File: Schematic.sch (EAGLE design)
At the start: 63 parts, among them IC1 7812, IC2 LM358N, Q1 IRF3205, Q2 IRF3205, Q3 IRF3205, Q4 IRF3205, Q5 IRF3205, Q6 IRF3205, Q7 IRF3205, Q8 IRF3205, X1 12Vcc IN, X2 MOTOR DC, X3 Resistencia Shunt

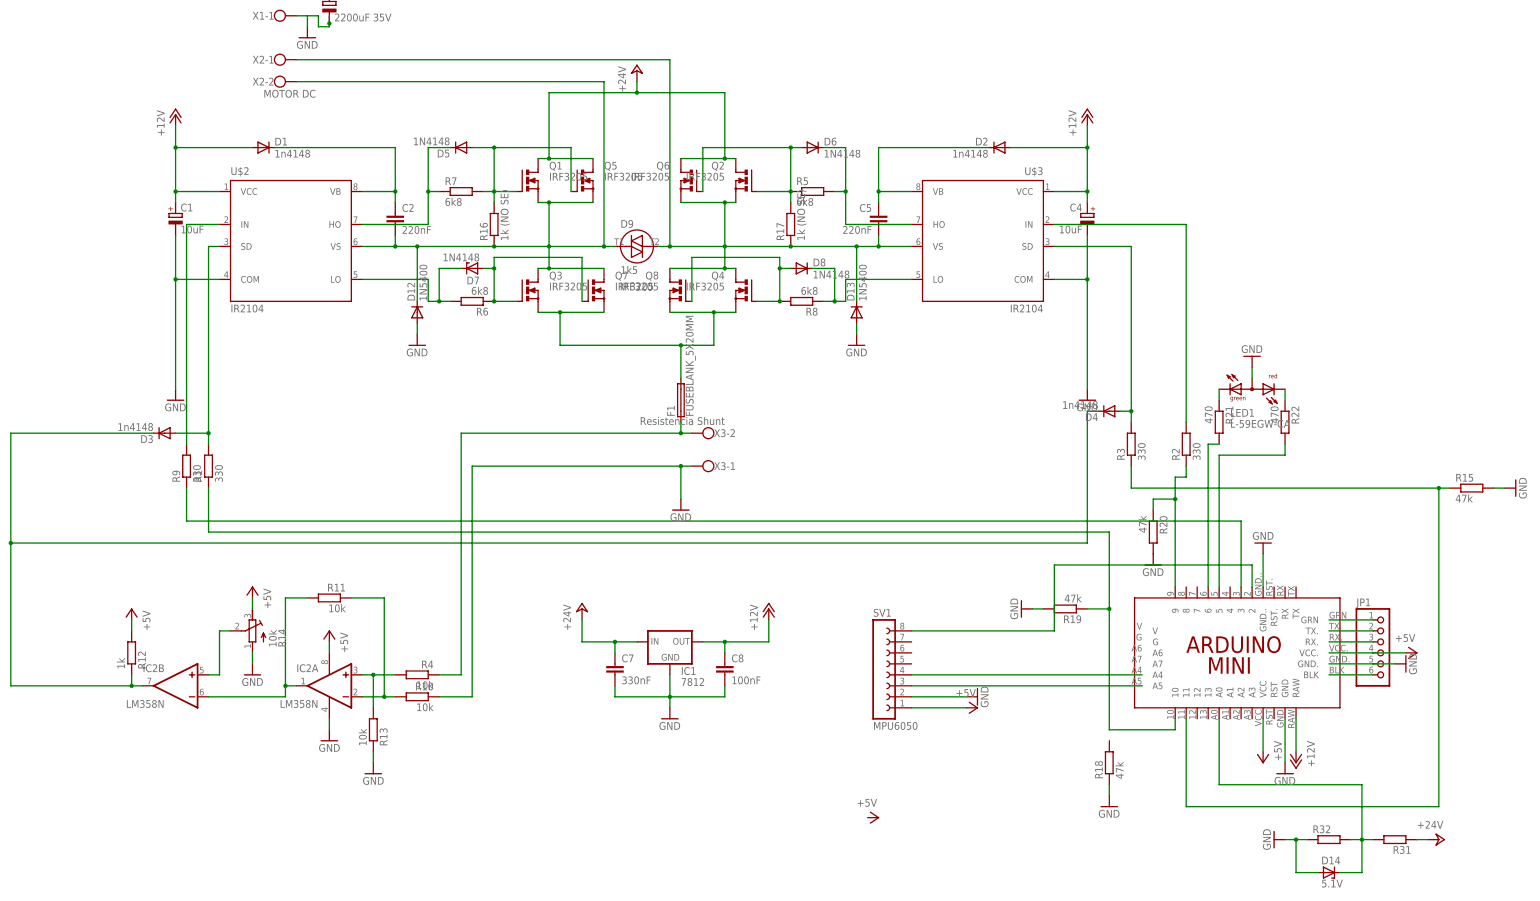
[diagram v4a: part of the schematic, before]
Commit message: Ver 6
Board: I added some shunt diodes to avoid voltage spikes that could burn out the circuit.
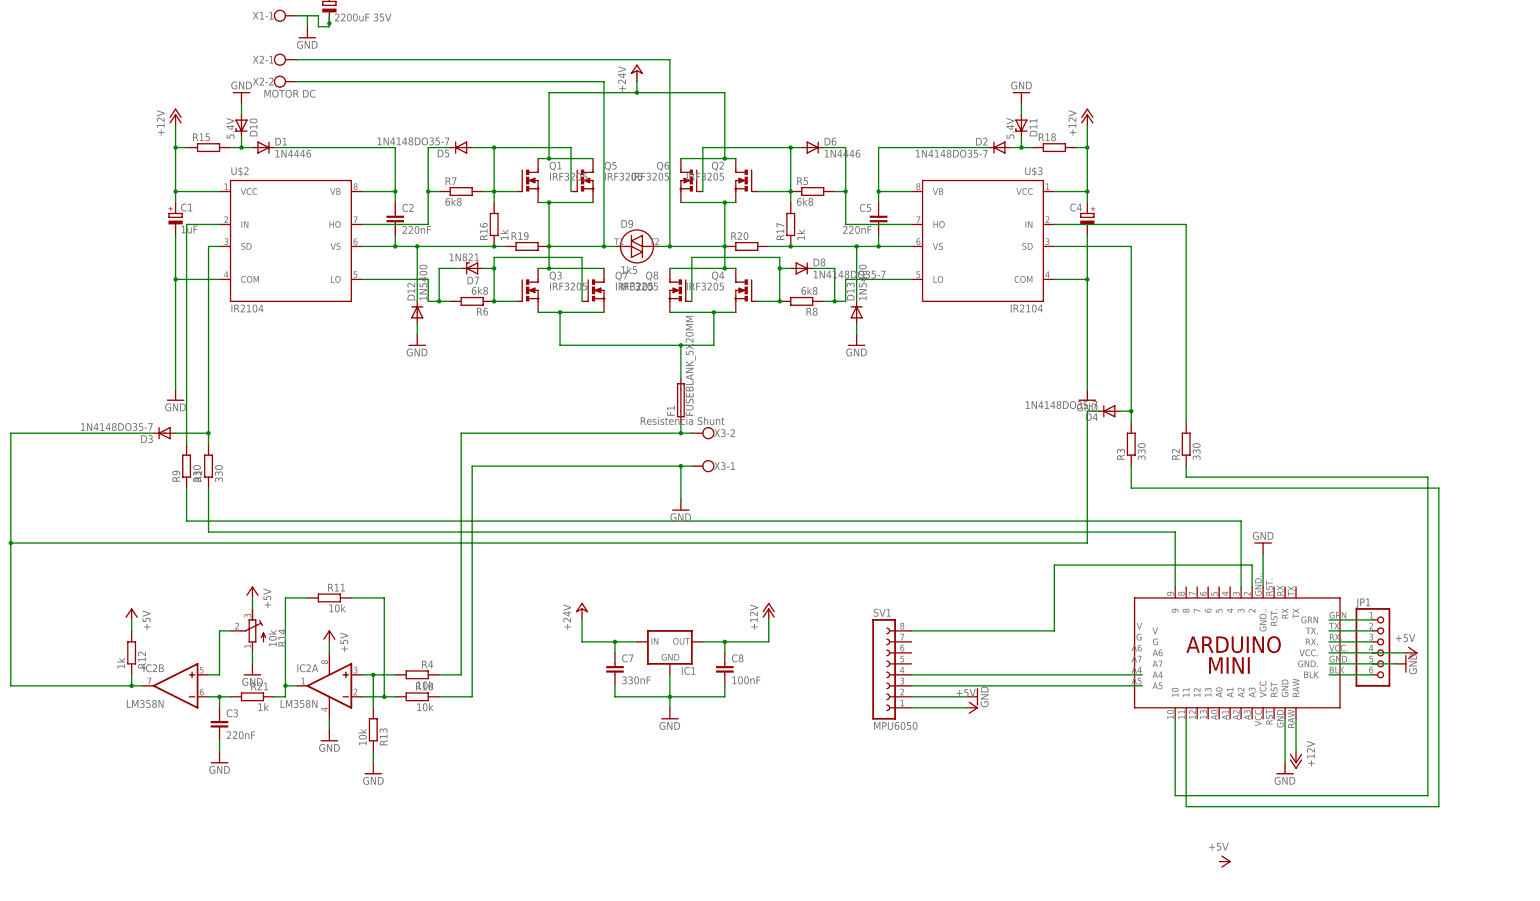
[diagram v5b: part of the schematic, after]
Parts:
- removed D14: 5.1V, diode Victor:ZENER-DIODEDO34-7
- removed LED1: L-59EGW-CA, led:L-59EGW-CA
- removed R22: 470, rcl:R-EU_0204/5
- removed R31, R32: (no value), rcl:R-EU_0204/5
- added C3: 220nF, rcl:C-EU075-032X103
- added D10, D11: 5.4V, diode Victor:ZENER-DIODEDO34-7
- C1: value 10uF -> 1uF
- C2, C5: device rcl:C-EU050-024X044 -> rcl:C-EU075-032X103
- C4: value 10uF -> (none)
- D1: value 1n4148 -> 1N4446
- D2, D3, D4: value 1n4148 -> 1N4148DO35-7
- D5, D8: value 1N4148 -> 1N4148DO35-7
- D6: value 1N4148 -> 1N4446
- D7: value 1N4148 -> 1N821
- IC1: value 7812 -> (none)
- R15, R18: value 47k -> (none); device rcl:R-EU_0204/5 -> rcl_Victor:R-EU_0204/7
- R16, R17: value 1k (NO SE) -> 1k
- R19, R20: value 47k -> (none); device rcl:R-EU_0204/5 -> rcl_Victor:R-EU_0207/15
- R21: value 470 -> 1k; device rcl:R-EU_0204/5 -> rcl_Victor:R-EU_0204/7
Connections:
- removed net N$30: LED1.CG, R21.1
- removed net N$61: D14.C, R31.2, R32.2, U$1.A0
- new net N$35: D9.T1, Q1.S, Q3.D, Q5.S, Q7.D, R19.2, X2-2.KL
- new net N$36: C5.2, D13.C, R17.1, R20.2, U$3.VS
- net +12V: now also R15.1, R18.2; no longer D1.A, D2.A
- net +24V: no longer R31.1
- net +5V: no longer U$1.VCC
- net GND: now also C3.2, D10.A, D11.A; no longer D14.A, LED1.A, R15.2, R18.1, R19.2, R20.2, R32.1
- net N$13: now also R19.1; no longer D9.T1, Q1.S, Q3.D, Q5.S, Q7.D, X2-2.KL
- net N$16: now also C3.1, IC2B.-IN, R21.2; no longer LED1.CR, R22.1
- net N$17: now also D1.A, D10.C, R15.2; no longer R21.2, U$1.6
- net N$19: now also R2.1, U$1.10; no longer R22.2, U$1.5
- net N$22: now also R21.1; no longer IC2B.-IN
- net N$29: now also D11.C, D2.A, R18.1; no longer R2.1, R20.1, U$1.9
- net N$33: no longer R15.1
- net N$34: now also R20.1; no longer C5.2, D13.C, R17.1, U$3.VS
- net N$7: now also U$1.9; no longer R19.1, U$1.10
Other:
- moved on the sheet: R15, R18, R19, R20, R21

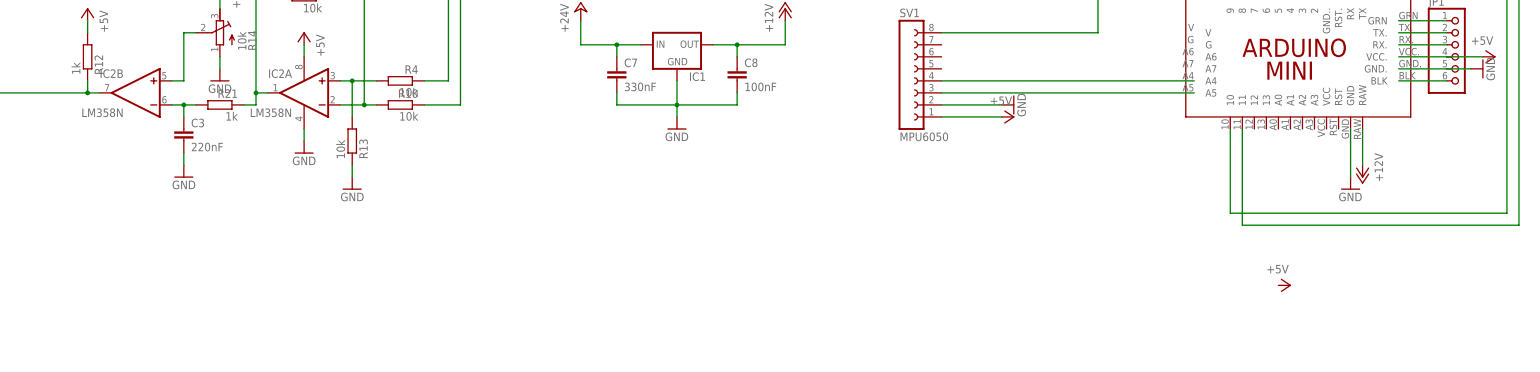
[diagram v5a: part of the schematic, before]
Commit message: Ver 7
Board: Some mixed improvements:
Algorithm: I needed to invert the X and Y axis.
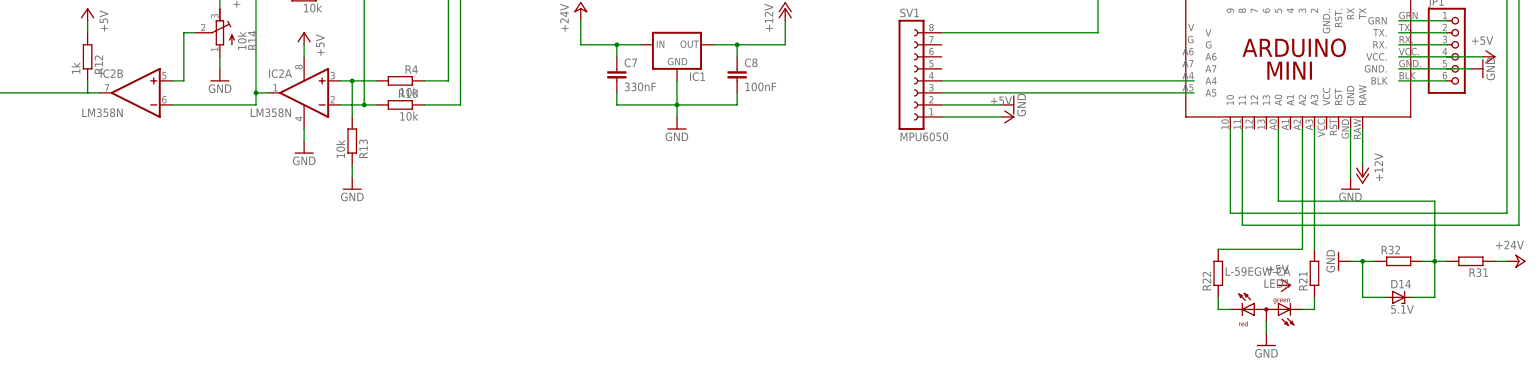
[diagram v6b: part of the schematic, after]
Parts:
- removed C3: 220nF, rcl:C-EU075-032X103
- added D14: 5.1V, diode Victor:ZENER-DIODEDO34-7
- added LED1: L-59EGW-CA, led:L-59EGW-CA
- added R22, R31, R32: (no value), rcl:R-EU_0204/5
- R21: value 1k -> (none); device rcl_Victor:R-EU_0204/7 -> rcl:R-EU_0204/5
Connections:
- new net N$30: LED1.CG, R21.1
- new net N$38: R21.2, U$1.A3
- new net N$39: R22.2, U$1.A2
- new net N$61: D14.C, R31.2, R32.2, U$1.A0
- net +24V: now also R31.1
- net GND: now also D14.A, LED1.A, R32.1; no longer C3.2
- net N$16: now also LED1.CR, R22.1; no longer C3.1, IC2B.-IN, R21.2
- net N$22: now also IC2B.-IN; no longer R21.1
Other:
- moved on the sheet: R21
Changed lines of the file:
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@@
 <part name="GND14" library="supply1" deviceset="GND" device=""/>
 <part name="GND17" library="supply1" deviceset="GND" device=""/>
-<part name="R21" library="rcl_Victor" deviceset="R-EU_" device="0204/7" value="1k"/>
-<part name="C3" library="rcl" deviceset="C-EU" device="075-032X103" value="220nF"/>
+<part name="R21" library="rcl" deviceset="R-EU_" device="0204/5"/>
+<part name="R22" library="rcl" deviceset="R-EU_" device="0204/5"/>
 <part name="GND2" library="supply1" deviceset="GND" device=""/>
+<part name="R31" library="rcl" deviceset="R-EU_" device="0204/5"/>
+<part name="R32" library="rcl" deviceset="R-EU_" device="0204/5"/>
+<part name="D14" library="diode Victor" deviceset="ZENER-DIODE" device="DO34-7" value="5.1V"/>
+<part name="P+12" library="supply1" deviceset="+24V" device=""/>
+<part name="GND18" library="supply1" deviceset="GND" device=""/>
+<part name="LED1" library="led" deviceset="L-59EGW-CA" device=""/>
 </parts>
 <sheets>
@@
 <instance part="GND14" gate="1" x="22.86" y="5.08"/>
 <instance part="GND17" gate="1" x="124.46" y="5.08"/>
-<instance part="R21" gate="G$1" x="-15.24" y="-76.2" rot="MR0"/>
-<instance part="C3" gate="G$1" x="-22.86" y="-81.28"/>
-<instance part="GND2" gate="1" x="-22.86" y="-91.44" rot="MR0"/>
+<instance part="R21" gate="G$1" x="215.9" y="-111.76" rot="R90"/>
+<instance part="R22" gate="G$1" x="195.58" y="-111.76" rot="R90"/>
+<instance part="GND2" gate="1" x="205.74" y="-127" rot="MR0"/>
+<instance part="R31" gate="G$1" x="248.92" y="-109.22" rot="R180"/>
+<instance part="R32" gate="G$1" x="233.68" y="-109.22"/>
+<instance part="D14" gate="G$1" x="233.68" y="-116.84"/>
+<instance part="P+12" gate="1" x="259.08" y="-109.22" rot="R270"/>
+<instance part="GND18" gate="1" x="220.98" y="-109.22" rot="R270"/>
+<instance part="LED1" gate="G$1" x="205.74" y="-119.38" rot="R90"/>
 </instances>
 <busses>
@@
 </segment>
 <segment>
+<pinref part="R32" gate="G$1" pin="1"/>
+<pinref part="GND18" gate="1" pin="GND"/>
+<wire x1="223.52" y1="-109.22" x2="226.06" y2="-109.22" width="0.1524" layer="91"/>
+<pinref part="D14" gate="G$1" pin="A"/>
+<wire x1="226.06" y1="-109.22" x2="228.6" y2="-109.22" width="0.1524" layer="91"/>
+<wire x1="231.14" y1="-116.84" x2="226.06" y2="-116.84" width="0.1524" layer="91"/>
+<wire x1="226.06" y1="-116.84" x2="226.06" y2="-109.22" width="0.1524" layer="91"/>
+<junction x="226.06" y="-109.22"/>
+</segment>
+<segment>
 <pinref part="GND2" gate="1" pin="GND"/>
-<pinref part="C3" gate="G$1" pin="2"/>
-<wire x1="-22.86" y1="-88.9" x2="-22.86" y2="-86.36" width="0.1524" layer="91"/>
+<pinref part="LED1" gate="G$1" pin="A"/>
+<wire x1="205.74" y1="-124.46" x2="205.74" y2="-121.92" width="0.1524" layer="91"/>
 </segment>
 </net>
@@
 <wire x1="83.82" y1="48.26" x2="93.98" y2="48.26" width="0.1524" layer="91"/>
 </segment>
+<segment>
+<pinref part="R31" gate="G$1" pin="1"/>
+<pinref part="P+12" gate="1" pin="+24V"/>
+<wire x1="256.54" y1="-109.22" x2="254" y2="-109.22" width="0.1524" layer="91"/>
+</segment>
 </net>
 <net name="+12V" class="0">
@@
 <wire x1="-71.12" y1="-15.24" x2="-71.12" y2="-40.64" width="0.1524" layer="91"/>
 <junction x="-71.12" y="-40.64"/>
-<junction x="-43.18" y="-73.66"/>
 </segment>
 </net>
@@
 <wire x1="-7.62" y1="-73.66" x2="-5.08" y2="-73.66" width="0.1524" layer="91"/>
 <wire x1="-7.62" y1="-73.66" x2="-7.62" y2="-76.2" width="0.1524" layer="91"/>
+<pinref part="IC2" gate="B" pin="-IN"/>
+<wire x1="-7.62" y1="-76.2" x2="-25.4" y2="-76.2" width="0.1524" layer="91"/>
 <junction x="-7.62" y="-73.66"/>
-<pinref part="R21" gate="G$1" pin="1"/>
-<wire x1="-7.62" y1="-76.2" x2="-10.16" y2="-76.2" width="0.1524" layer="91"/>
 </segment>
 </net>
@@
 </segment>
 </net>
+<net name="N$61" class="0">
+<segment>
+<pinref part="R31" gate="G$1" pin="2"/>
+<pinref part="R32" gate="G$1" pin="2"/>
+<wire x1="238.76" y1="-109.22" x2="241.3" y2="-109.22" width="0.1524" layer="91"/>
+<pinref part="D14" gate="G$1" pin="C"/>
+<wire x1="241.3" y1="-109.22" x2="243.84" y2="-109.22" width="0.1524" layer="91"/>
+<wire x1="241.3" y1="-109.22" x2="241.3" y2="-116.84" width="0.1524" layer="91"/>
+<wire x1="241.3" y1="-116.84" x2="236.22" y2="-116.84" width="0.1524" layer="91"/>
+<wire x1="241.3" y1="-109.22" x2="241.3" y2="-96.52" width="0.1524" layer="91"/>
+<junction x="241.3" y="-109.22"/>
+<pinref part="U$1" gate="G$1" pin="A0"/>
+<wire x1="241.3" y1="-96.52" x2="208.28" y2="-96.52" width="0.1524" layer="91"/>
+<wire x1="208.28" y1="-96.52" x2="208.28" y2="-81.28" width="0.1524" layer="91"/>
+</segment>
+</net>
 <net name="N$16" class="0">
 <segment>
-<pinref part="C3" gate="G$1" pin="1"/>
-<wire x1="-22.86" y1="-78.74" x2="-22.86" y2="-76.2" width="0.1524" layer="91"/>
-<pinref part="IC2" gate="B" pin="-IN"/>
-<wire x1="-25.4" y1="-76.2" x2="-22.86" y2="-76.2" width="0.1524" layer="91"/>
+<pinref part="R22" gate="G$1" pin="1"/>
+<wire x1="195.58" y1="-116.84" x2="195.58" y2="-119.38" width="0.1524" layer="91"/>
+<pinref part="LED1" gate="G$1" pin="CR"/>
+<wire x1="195.58" y1="-119.38" x2="198.12" y2="-119.38" width="0.1524" layer="91"/>
+</segment>
+</net>
+<net name="N$30" class="0">
+<segment>
+<pinref part="LED1" gate="G$1" pin="CG"/>
+<pinref part="R21" gate="G$1" pin="1"/>
+<wire x1="213.36" y1="-119.38" x2="215.9" y2="-119.38" width="0.1524" layer="91"/>
+<wire x1="215.9" y1="-119.38" x2="215.9" y2="-116.84" width="0.1524" layer="91"/>
+</segment>
+</net>
+<net name="N$39" class="0">
+<segment>
+<pinref part="R22" gate="G$1" pin="2"/>
+<wire x1="195.58" y1="-106.68" x2="213.36" y2="-106.68" width="0.1524" layer="91"/>
+<pinref part="U$1" gate="G$1" pin="A2"/>
+<wire x1="213.36" y1="-81.28" x2="213.36" y2="-106.68" width="0.1524" layer="91"/>
+</segment>
+</net>
+<net name="N$38" class="0">
+<segment>
 <pinref part="R21" gate="G$1" pin="2"/>
-<wire x1="-20.32" y1="-76.2" x2="-22.86" y2="-76.2" width="0.1524" layer="91"/>
-<junction x="-22.86" y="-76.2"/>
-</segment>
-</net>
+<pinref part="U$1" gate="G$1" pin="A3"/>
+<wire x1="215.9" y1="-106.68" x2="215.9" y2="-81.28" width="0.1524" layer="91"/>
+</segment>
+</net>
